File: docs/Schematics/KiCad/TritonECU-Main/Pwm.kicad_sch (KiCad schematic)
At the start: 36 parts, among them Q501 NCV8405ASTT1G, Q502 NCV8405ASTT1G, Q503 NCV8405ASTT1G, Q504 NCV8408BDTRKG, Q505 NCV8405ASTT1G, Q506 NCV8405ASTT1G, Q507 NCV8405ASTT1G, U501 74HCT541

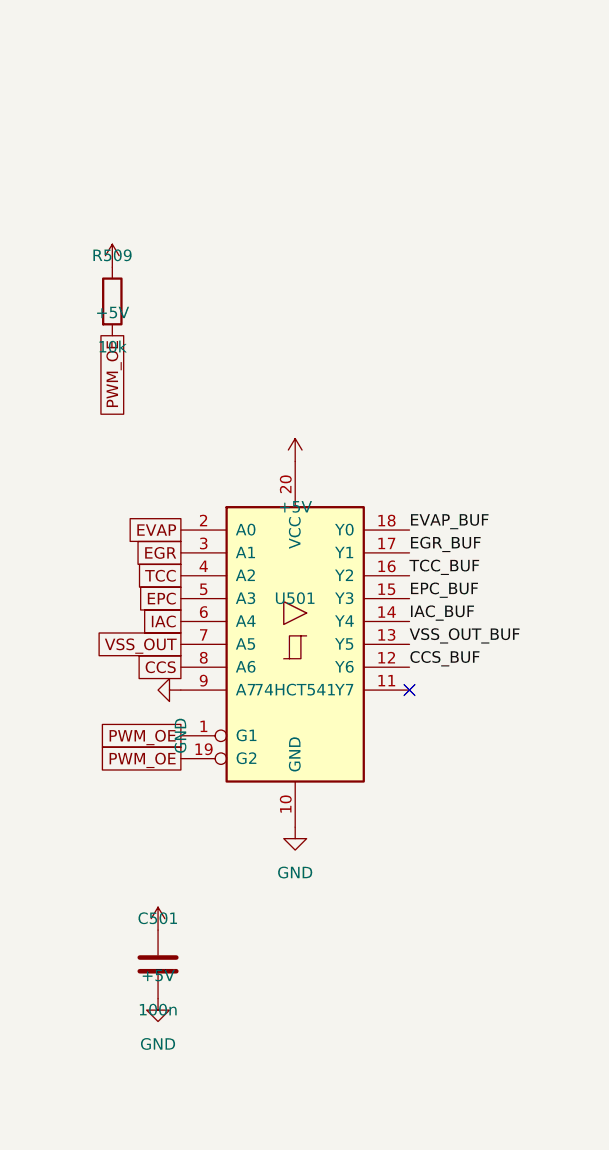
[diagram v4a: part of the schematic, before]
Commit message: Carrier: Inputs sheet and switched rails for sleep
Inputs: one network per switch input - 4.7k pull-up to VPWR (ground-
switched only; VPWR so a TR bit closed in Park draws nothing parked),
SMF24A, 33k/15k, 10n, BAT54J to 3.3 V. TR1/2/4 and 4X4L ground-switched,
TR3A/BRAKE/ACP/TCS 12 V high-side. 4X4L mapped to EEC-V pin 14
(findings sec.14). IGN_WAKE from VPWR into PC13/WKUP4. TACH/SPEED bench
header, BOOT0 DFU solder jumper.

Switched rails: +5V and +3.3V stay up parked, so two TPS22917 load
switches on SW_RAIL_EN (PG12, 100k down) make +5V_SW / +3.3V_SW for the
running-only loads: 74HCT541 x3 and OE pull-ups, MAX9926 x3 and COUT
pull-ups, ADS8588H, OPA2376 x2, O2 bias, knock block, 74HC4051, TPS2H160B
FAULT pull-up, TFT pull-up. MCU, watchdog, CAN, SCP RX, clamps stay on.

gen_carrier_pcb.py: packer steps around existing parts, fills several
rects in turn, parks overflow below earlier parked parts.

Co-Authored-By: Claude Opus 5.5 <noreply@anthropic.com>
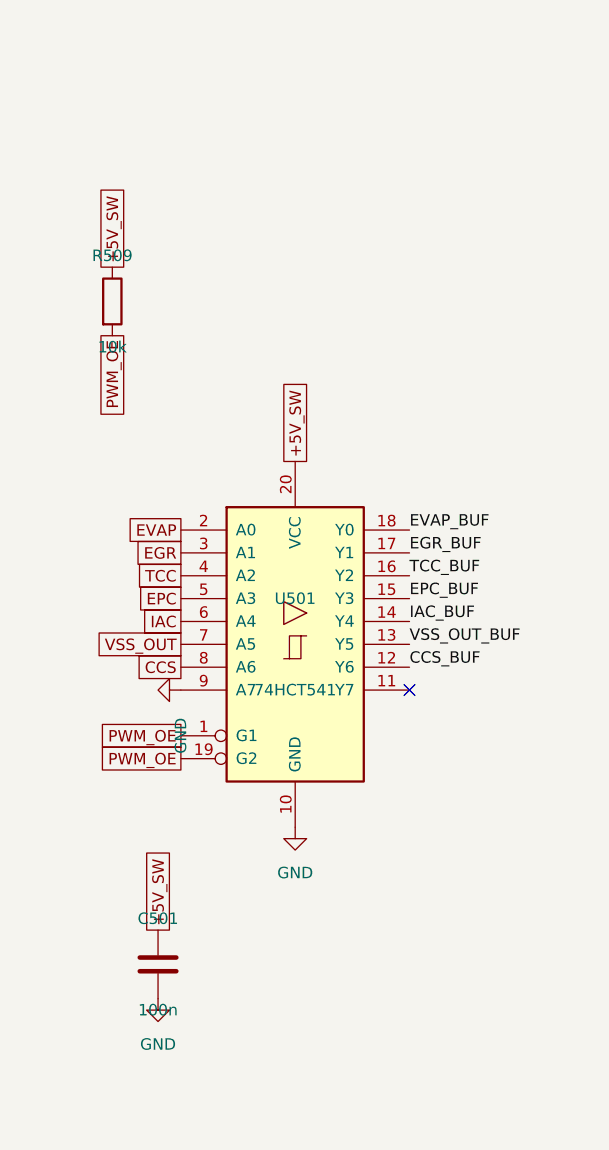
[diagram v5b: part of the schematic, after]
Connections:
- net +5V: no longer C501.1, R509.1, U501.20 (VCC)
- new net +5V_SW: C501.1, R509.1, U501.20 (VCC)
